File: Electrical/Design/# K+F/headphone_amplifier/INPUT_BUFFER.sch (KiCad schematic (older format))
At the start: 20 parts

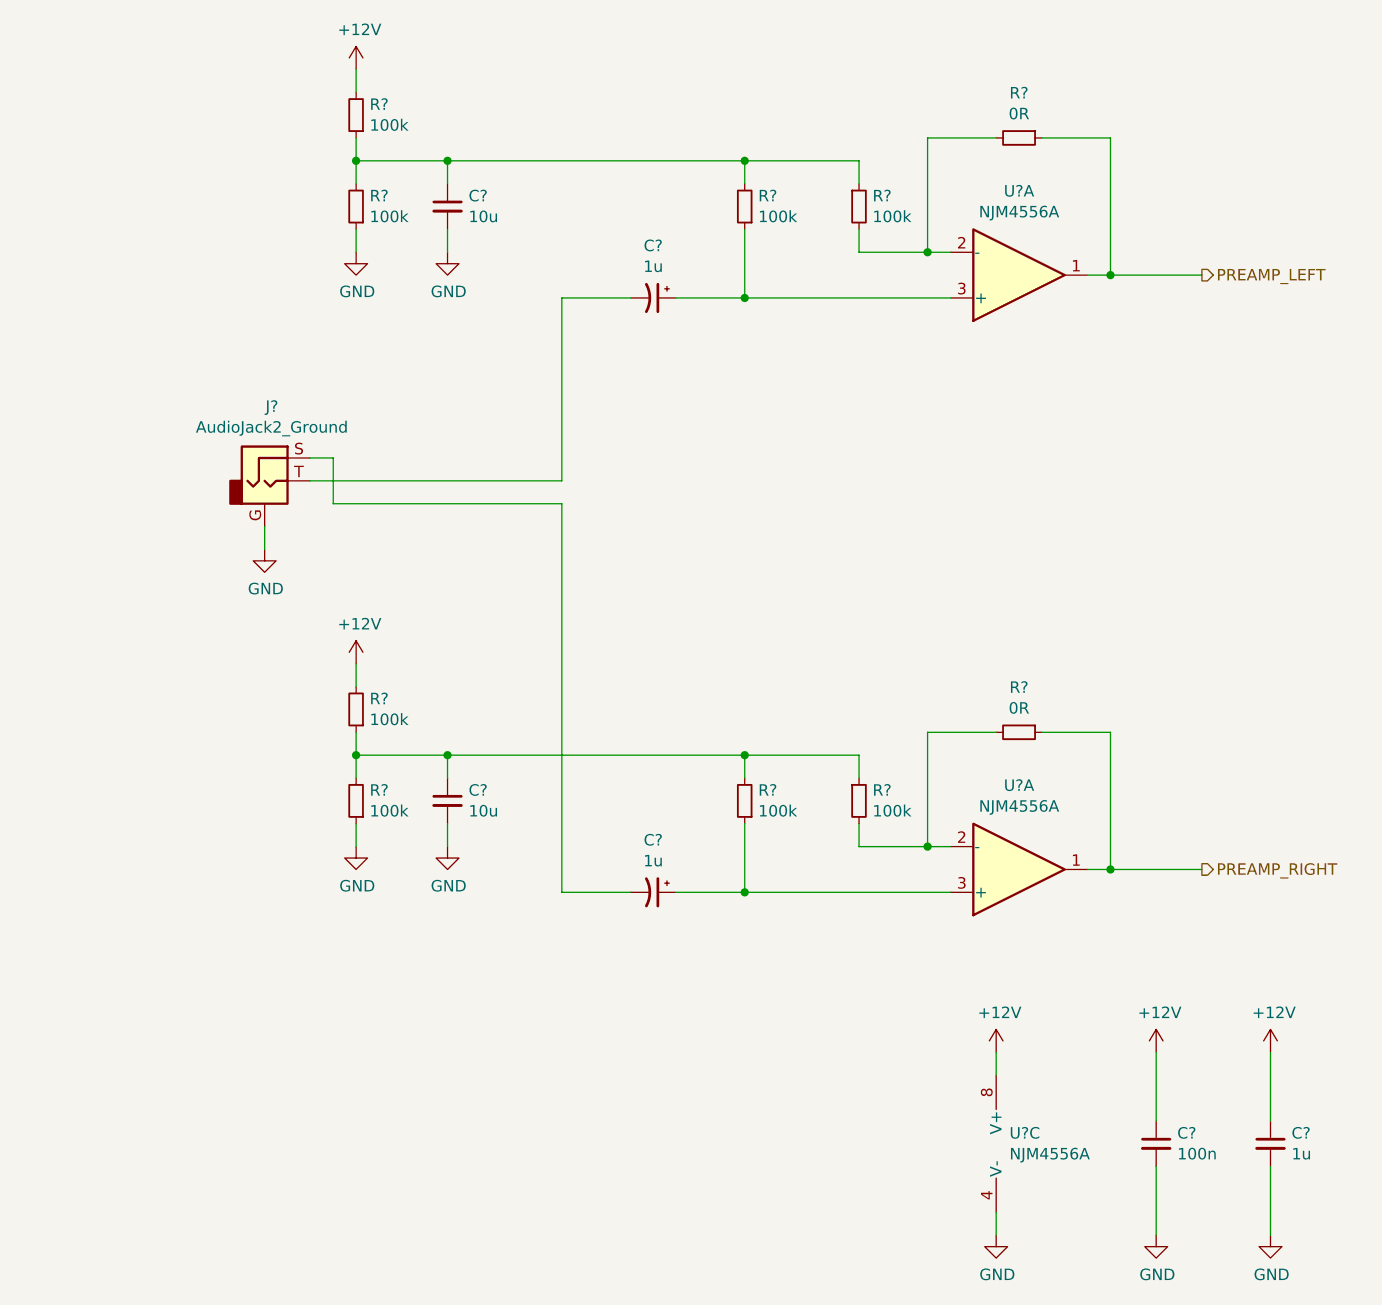
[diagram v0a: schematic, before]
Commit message: SUKU headphone_amplifier schematic fix and simulation added
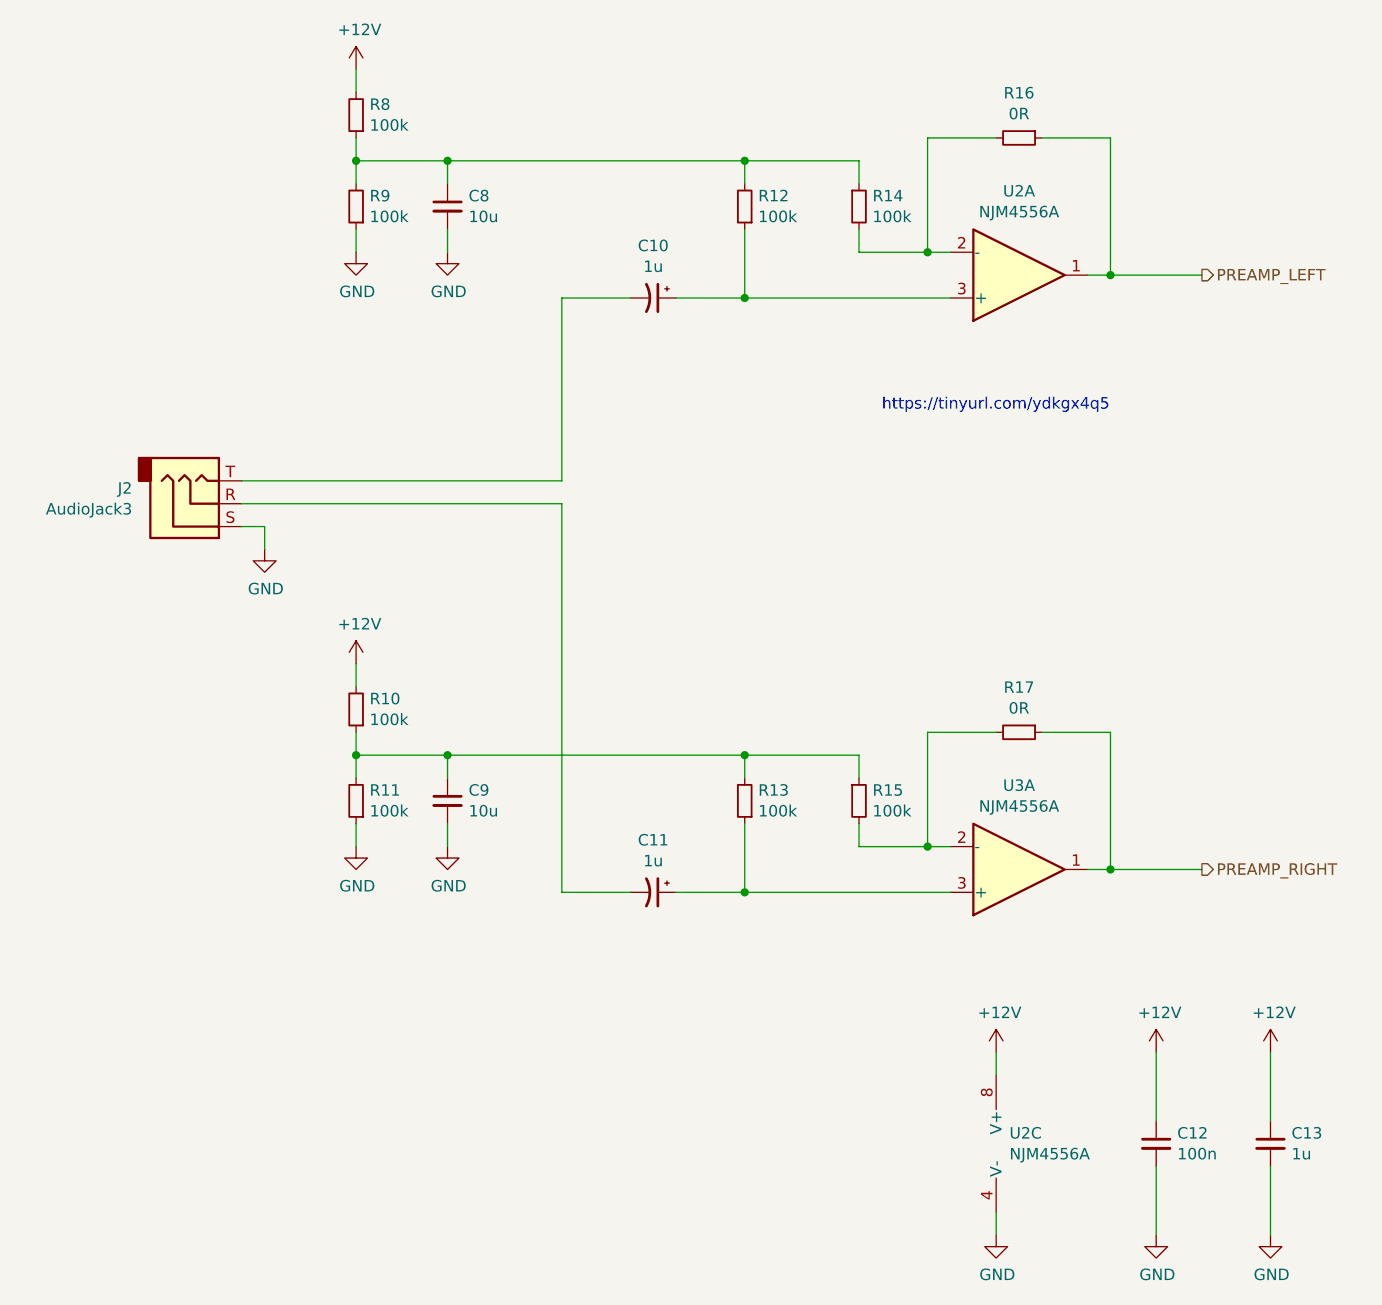
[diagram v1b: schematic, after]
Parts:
- removed J?: AudioJack2_Ground, symbol Connector:AudioJack2_Ground
- added J2: AudioJack3, suku_basics:jack_3.5_vertical_stereo, symbol Connector:AudioJack3
- C10, C11: renamed from C?; footprint (none) -> Capacitor_SMD:CP_Elec_4x5.4
- gave numbers to parts that had none: 16
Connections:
- net GND: now also J2.S
- net at C10.2: now also J2.T
- net at C11.2: now also J2.R
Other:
- note added: "https://tinyurl.com/ydkgx4q5"
